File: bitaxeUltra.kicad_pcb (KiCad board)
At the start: 4 copper layers, 56.5 x 99.8 mm, 143 parts, among them J1 54-00164, J10 Conn_01x02, J2 Conn_01x02, J3 Conn_01x05, J4 Conn_01x04, J5 TC2030-IDC, J6 Conn_01x04, J7 Conn_01x02, J8 USB_C_Receptacle_USB2.0, J9 Conn_01x04, Q1 CSD17311Q5, Q2 CSD17311Q5, Q4 2N7002K, SW1 GT-TC029B-H025-L1N, SW2 GT-TC029B-H025-L1N, U1 25MHz, U10 DS4432U+, U11 RT9080-33GJ5, U12 ESP32-S3-WROOM-1, U14 BM1366_mode1, U2 TXB0104RGYR, U5 MCP1824T-1802E, U6 MCP1824T-0802E, U7 EMC2101, U8 INA260, U9 TPS40305, Y1 32.768kHz

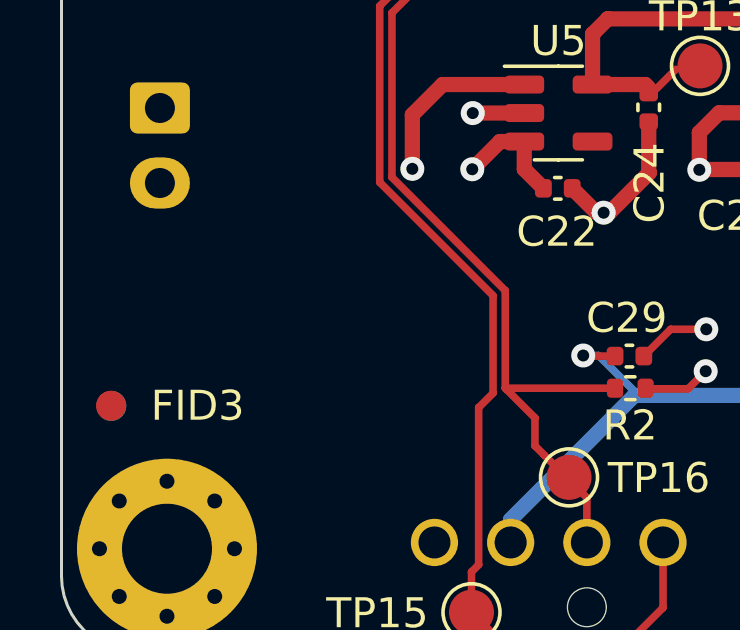
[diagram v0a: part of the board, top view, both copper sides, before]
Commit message: added 3rs heatsink mounting hole
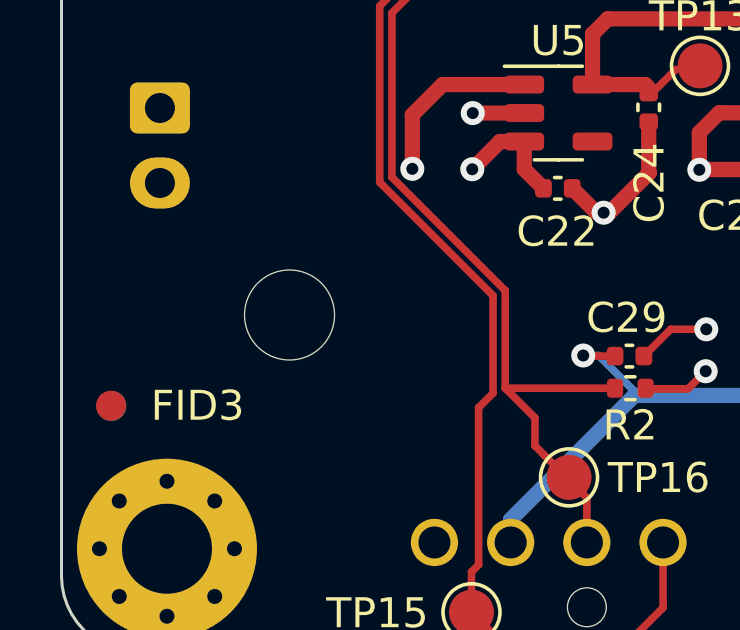
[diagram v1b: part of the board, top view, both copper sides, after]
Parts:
- added ?: , , F.Cu at (84.8, 136.0)
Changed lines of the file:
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@@
+		)
+	)
+	(footprint ""
+		(layer "F.Cu")
+		(at 84.79 136.04)
+		(property "Reference" ""
+			(at 0 0 0)
+			(layer "F.SilkS")
+			(effects
+				(font
+					(size 1.27 1.27)
+					(thickness 0.15)
+				)
+			)
+		)
+		(property "Value" ""
+			(at 0 0 0)
+			(layer "F.Fab")
+			(effects
+				(font
+					(size 1.27 1.27)
+					(thickness 0.15)
+				)
+			)
+		)
+		(property "Footprint" ""
+			(at 0 0 0)
+			(layer "F.Fab")
+			(hide yes)
+			(effects
+				(font
+					(size 1.27 1.27)
+					(thickness 0.15)
+				)
+			)
+		)
+		(property "Datasheet" ""
+			(at 0 0 0)
+			(layer "F.Fab")
+			(hide yes)
+			(effects
+				(font
+					(size 1.27 1.27)
+					(thickness 0.15)
+				)
+			)
+		)
+		(property "Description" ""
+			(at 0 0 0)
+			(layer "F.Fab")
+			(hide yes)
+			(effects
+				(font
+					(size 1.27 1.27)
+					(thickness 0.15)
+				)
+			)
+		)
+		(pad "" np_thru_hole circle
+			(at 0 0)
+			(size 3 3)
+			(drill 3)
+			(layers "F&B.Cu" "*.Mask")
 		)
 	)

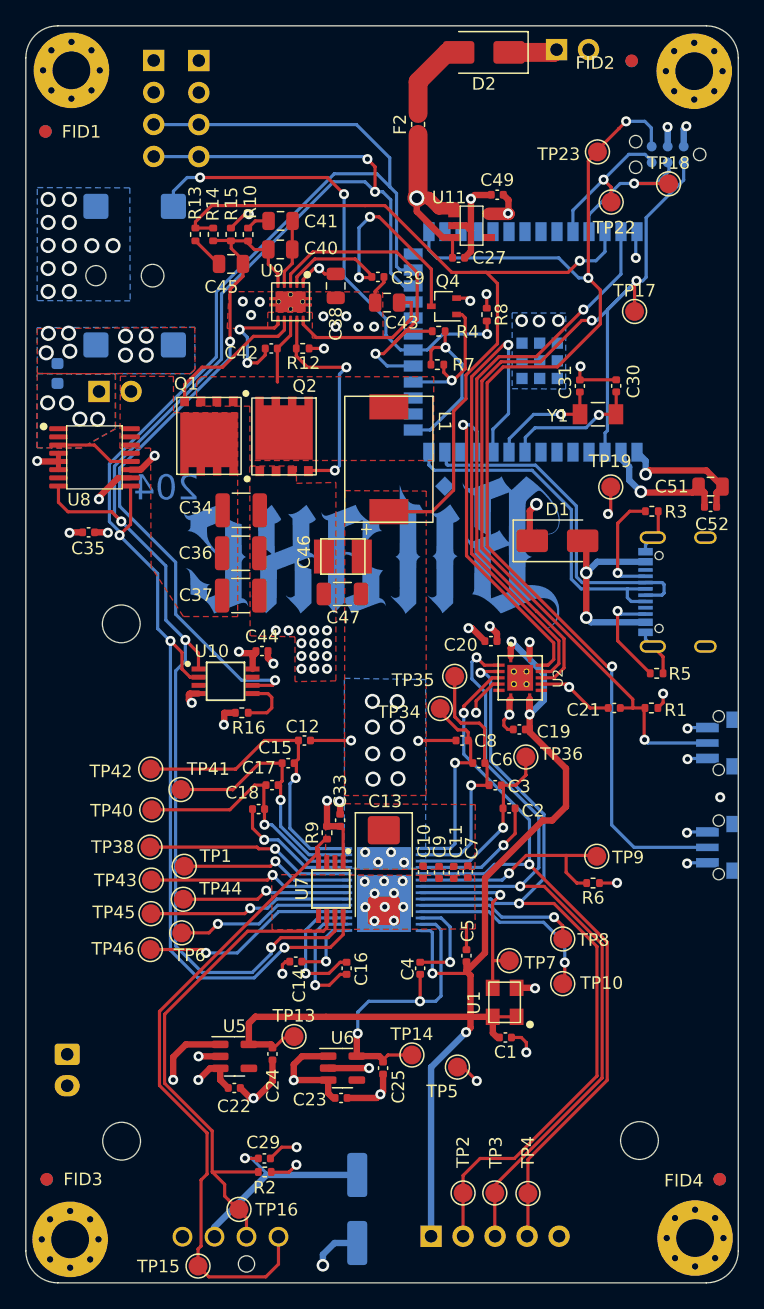
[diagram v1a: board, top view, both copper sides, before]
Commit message: added sda and scl puulups
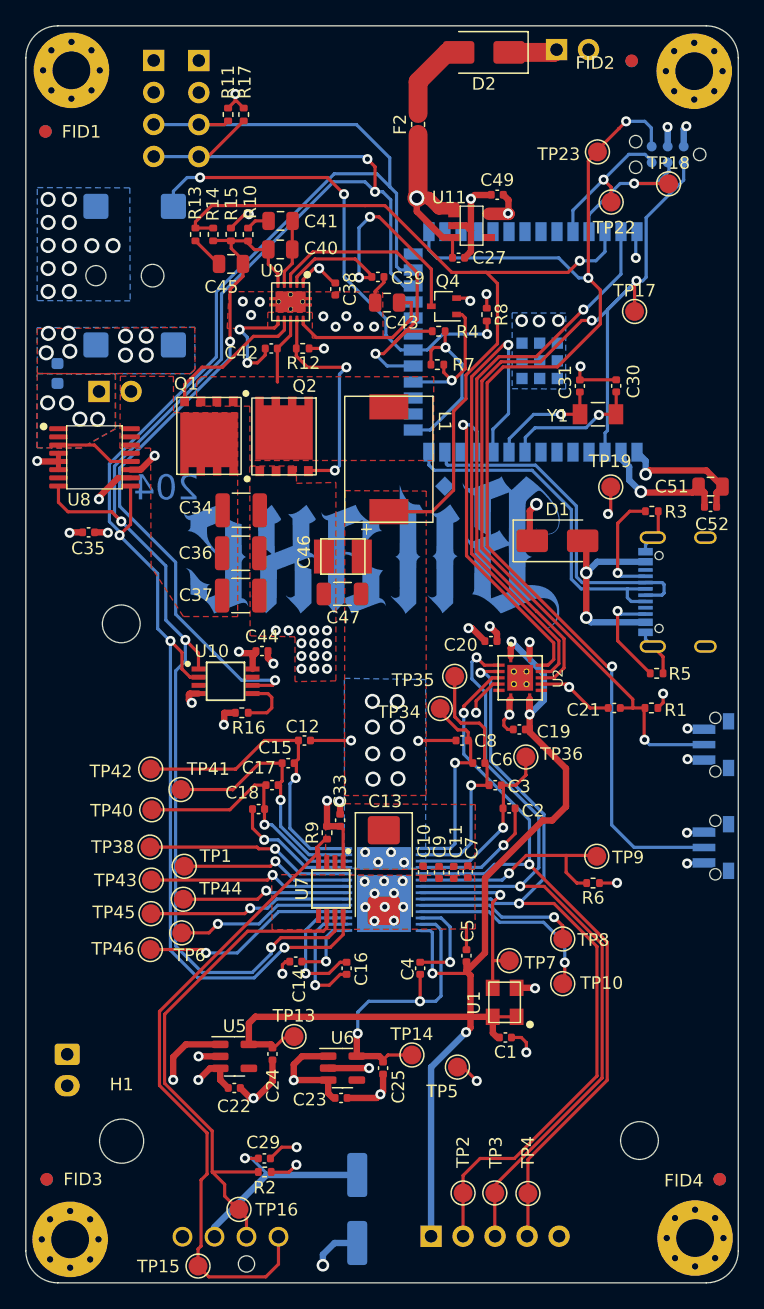
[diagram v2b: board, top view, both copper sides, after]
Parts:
- removed ?: , 
- added H1: MountingHole, MountingHole:MountingHole_3.5mm, F.Cu at (84.8, 136.0)
- added R11: 4.7k, Resistor_SMD:R_0402_1005Metric, F.Cu at (93.2, 54.6)
- added R17: 4.7k, Resistor_SMD:R_0402_1005Metric, F.Cu at (94.5, 54.6)
- C38: footprint Capacitor_SMD:C_0805_2012Metric -> Capacitor_SMD:C_0402_1005Metric
- moved SW1 0.30 mm to (131.9, 104.6)
- moved SW2 0.27 mm to (131.9, 112.7)
- moved C38 0.25 mm to (101.8, 68.4)
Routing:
- net /SDA: track 129.5 -> 134.2 mm
- net /3V3: track 75.8 -> 78.6 mm, vias 14 -> 15
- net /SCL: track 131.9 -> 134.4 mm
- net GND: track 147.2 -> 146.1 mm, vias 86 -> 85
- net /BM1366/RO: track 66.2 -> 65.5 mm
- net /ESP32/IO0: track 95.2 -> 94.6 mm

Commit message: small tweak
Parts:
- moved R11 0.58 mm to (93.3, 54.0)
- moved R17 0.57 mm to (94.4, 54.0)
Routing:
- net /3V3: track 78.6 -> 77.4 mm
- net /SDA: track 134.2 -> 134.8 mm
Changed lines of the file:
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@@
 	(footprint "Resistor_SMD:R_0402_1005Metric"
 		(layer "F.Cu")
-		(at 94.48 54.56 90)
+		(at 94.42 53.99 90)
 		(descr "Resistor SMD 0402 (1005 Metric), square (rectangular) end terminal, IPC_7351 nominal, (Body size source: IPC-SM-782 page 72, https://www.pcb-3d.com/wordpress/wp-content/uploads/ipc-sm-782a_amendment_1_and_2.pdf), generated with kicad-footprint-generator")
 		(tags "resistor")
 		(property "Reference" "R17"
-			(at 2.58 0.08 90)
+			(at 2.59 0.14 90)
 			(layer "F.SilkS")
 			(effects
@@
 	(footprint "Resistor_SMD:R_0402_1005Metric"
 		(layer "F.Cu")
-		(at 93.24 54.56 90)
+		(at 93.27 53.98 90)
 		(descr "Resistor SMD 0402 (1005 Metric), square (rectangular) end terminal, IPC_7351 nominal, (Body size source: IPC-SM-782 page 72, https://www.pcb-3d.com/wordpress/wp-content/uploads/ipc-sm-782a_amendment_1_and_2.pdf), generated with kicad-footprint-generator")
 		(tags "resistor")
@@
 	)
 	(segment
-		(start 93.82 53.39)
+		(start 94.37 53.48)
 		(end 93.82 52.93)
 		(width 0.254)
@@
 	)
 	(segment
-		(start 93.24 54.05)
-		(end 93.82 53.47)
-		(width 0.254)
-		(layer "F.Cu")
-		(net 8)
-	)
-	(segment
 		(start 115.493 61.343)
 		(end 115.08 60.93)
@@
 	)
 	(segment
-		(start 93.82 53.47)
-		(end 93.82 52.93)
-		(width 0.254)
-		(layer "F.Cu")
-		(net 8)
-	)
-	(segment
 		(start 95.19 98.565)
 		(end 95.19 97.56)
@@
 	)
 	(segment
+		(start 94.42 53.48)
+		(end 94.37 53.48)
+		(width 0.254)
+		(layer "F.Cu")
+		(net 8)
+	)
+	(segment
 		(start 113.94095 62.4402)
 		(end 115.4928 62.4402)
@@
 	)
 	(segment
-		(start 82.99 84.925)
-		(end 84.52 83.395)
-		(width 0.508)
+		(start 93.28 53.47)
+		(end 93.82 52.93)
+		(width 0.254)
 		(layer "F.Cu")
 		(net 8)
 	)
 	(segment
-		(start 94.48 54.05)
-		(end 93.82 53.39)
-		(width 0.254)
+		(start 82.99 84.925)
+		(end 84.52 83.395)
+		(width 0.508)
 		(layer "F.Cu")
 		(net 8)
@@
 	)
 	(segment
+		(start 93.27 53.47)
+		(end 93.28 53.47)
+		(width 0.254)
+		(layer "F.Cu")
+		(net 8)
+	)
+	(segment
 		(start 131.05 85.7)
 		(end 131.05 84.56)
@@
 	)
 	(segment
-		(start 93.79 52.9)
-		(end 91 52.9)
+		(start 93.82 52.93)
+		(end 93.85 52.9)
 		(width 1.5)
 		(layer "In2.Cu")
@@
 	)
 	(segment
-		(start 90.92 52.82)
-		(end 87.35 52.82)
+		(start 93.79 52.9)
+		(end 91 52.9)
 		(width 1.5)
 		(layer "In2.Cu")
@@
 	)
 	(segment
-		(start 93.85 52.9)
-		(end 93.82 52.93)
+		(start 109.13 52.9)
+		(end 111.16 54.93)
 		(width 1.5)
 		(layer "In2.Cu")
@@
 	)
 	(segment
-		(start 91 52.9)
-		(end 90.92 52.82)
+		(start 90.92 52.82)
+		(end 87.35 52.82)
 		(width 1.5)
 		(layer "In2.Cu")
@@
 	)
 	(segment
-		(start 93.82 52.93)
-		(end 93.79 52.9)
+		(start 91 52.9)
+		(end 90.92 52.82)
 		(width 1.5)
 		(layer "In2.Cu")
@@
 	)
 	(segment
-		(start 109.13 52.9)
-		(end 93.85 52.9)
+		(start 93.85 52.9)
+		(end 109.13 52.9)
 		(width 1.5)
 		(layer "In2.Cu")
@@
 	)
 	(segment
-		(start 111.16 54.93)
-		(end 109.13 52.9)
+		(start 93.82 52.93)
+		(end 93.79 52.9)
 		(width 1.5)
 		(layer "In2.Cu")
@@
 	)
 	(segment
-		(start 101.36 120.659)
-		(end 102.3718 119.6472)
+		(start 93.27 54.49)
+		(end 92.4 55.36)
 		(width 0.254)
 		(layer "F.Cu")
@@
 	)
 	(segment
-		(start 89.58 98.5638)
-		(end 90.2312 99.215)
+		(start 101.36 120.659)
+		(end 102.3718 119.6472)
 		(width 0.254)
 		(layer "F.Cu")
@@
 	)
 	(segment
-		(start 93.24 55.07)
-		(end 92.95 55.36)
+		(start 89.58 98.5638)
+		(end 90.2312 99.215)
 		(width 0.254)
 		(layer "F.Cu")
@@
 	)
 	(segment
-		(start 92.95 55.36)
+		(start 92.4 55.36)
 		(end 90.92 55.36)
 		(width 0.254)
@@
 	)
 	(segment
+		(start 94.42 55.13)
+		(end 91.65 57.9)
+		(width 0.254)
+		(layer "F.Cu")
+		(net 64)
+	)
+	(segment
 		(start 89.85 96.26)
 		(end 90.89 97.3)
@@
 	)
 	(segment
-		(start 94.48 55.07)
-		(end 91.65 57.9)
+		(start 91.65 57.9)
+		(end 90.92 57.9)
 		(width 0.254)
 		(layer "F.Cu")
@@
 	)
 	(segment
+		(start 94.42 54.5)
+		(end 94.42 55.13)
+		(width 0.254)
+		(layer "F.Cu")
+		(net 64)
+	)
+	(segment
 		(start 101.186 119.888)
 		(end 101.7218 119.3522)
@@
 		(width 0.254)
 		(layer "F.Cu")
-		(net 64)
-	)
-	(segment
-		(start 91.65 57.9)
-		(end 90.92 57.9)
-		(width 0.254)
-		(layer "F.Cu")
